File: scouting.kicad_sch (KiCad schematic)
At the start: 57 parts, among them SW1 SW_DIP_x01, SW2 SW_DIP_x01, U1 ATmega328-P, U3 74HC138, Y1 Crystal

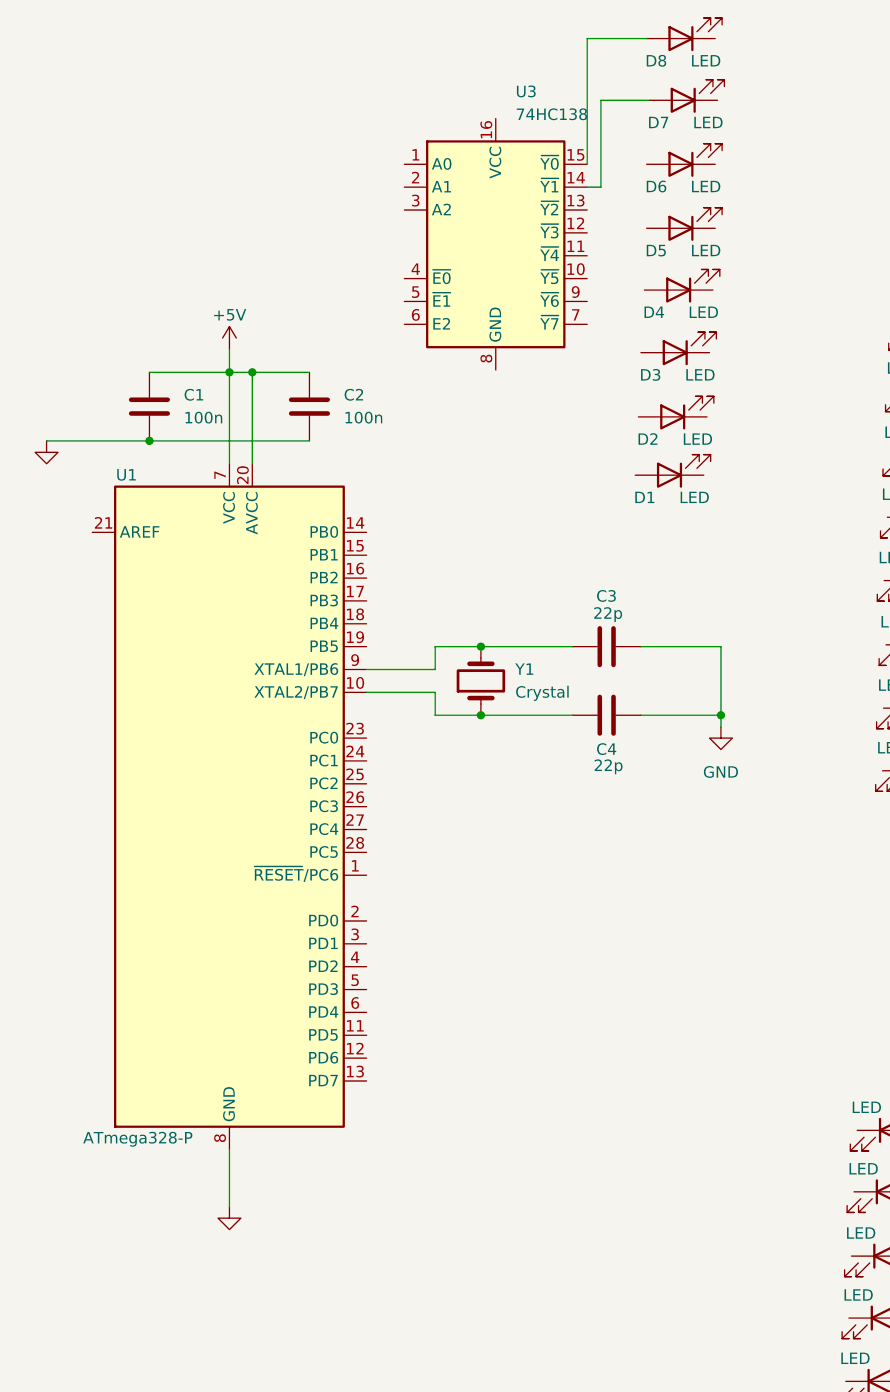
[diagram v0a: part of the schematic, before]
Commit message: Cleanup of schematic
Untangled supply wires, moved part of the LEDs to different sheet to have a nicer overview
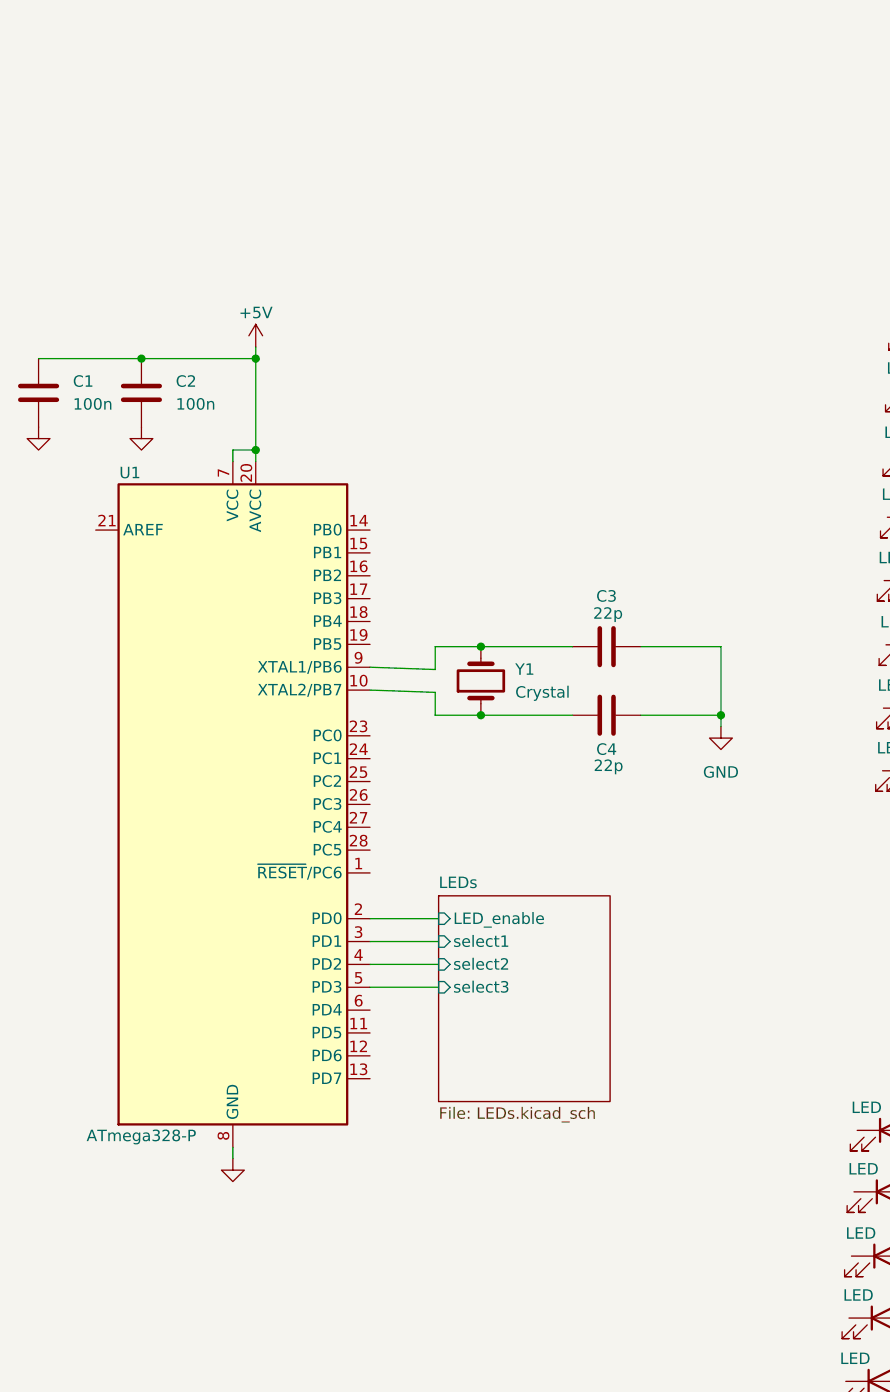
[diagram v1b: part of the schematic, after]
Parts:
- removed D1, D2, D3, D4, D5, D6, D7, D8: LED, symbol Device:LED
- removed U3: 74HC138, symbol 74xx:74HC138
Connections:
- net LEDs/LED_enable: now reaches U1.2 (PD0)
- net LEDs/select1: now reaches U1.3 (PD1)
- net LEDs/select2: now reaches U1.4 (PD2)
- net LEDs/select3: now reaches U1.5 (PD3)
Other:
- added sheet LEDs (LEDs.kicad_sch)
- moved on the sheet: C1, C2
